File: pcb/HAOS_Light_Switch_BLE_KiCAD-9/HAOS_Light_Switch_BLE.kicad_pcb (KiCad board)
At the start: 2 copper layers, 30.1 x 29.9 mm, 34 parts, among them J1 GPIO, J2 GPIO, J3 GPIO, J4 Battery_CR2032, J7 SWD, SW1 SW_Push, SW2 SW_Push, SW3 SW_Push, U1 nrf52832, U3 RF_Antenna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

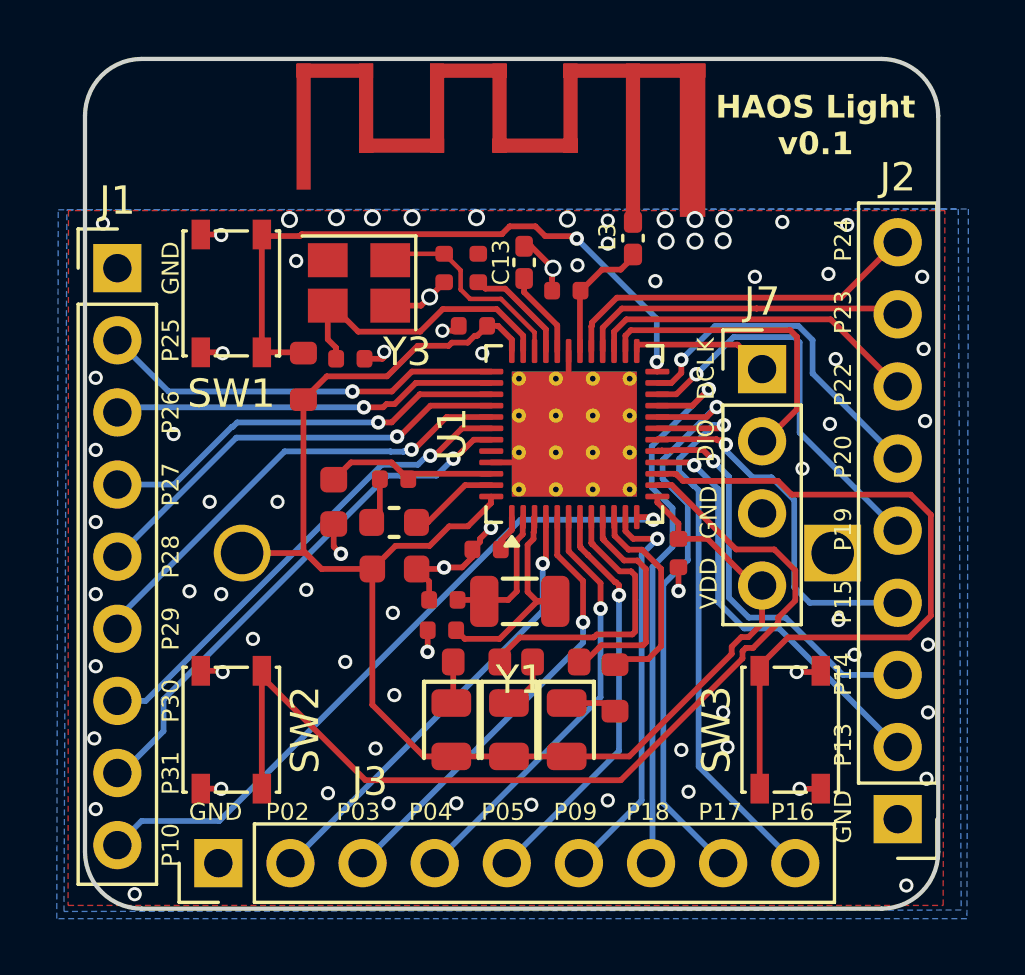
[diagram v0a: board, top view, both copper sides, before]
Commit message: Updated antenna
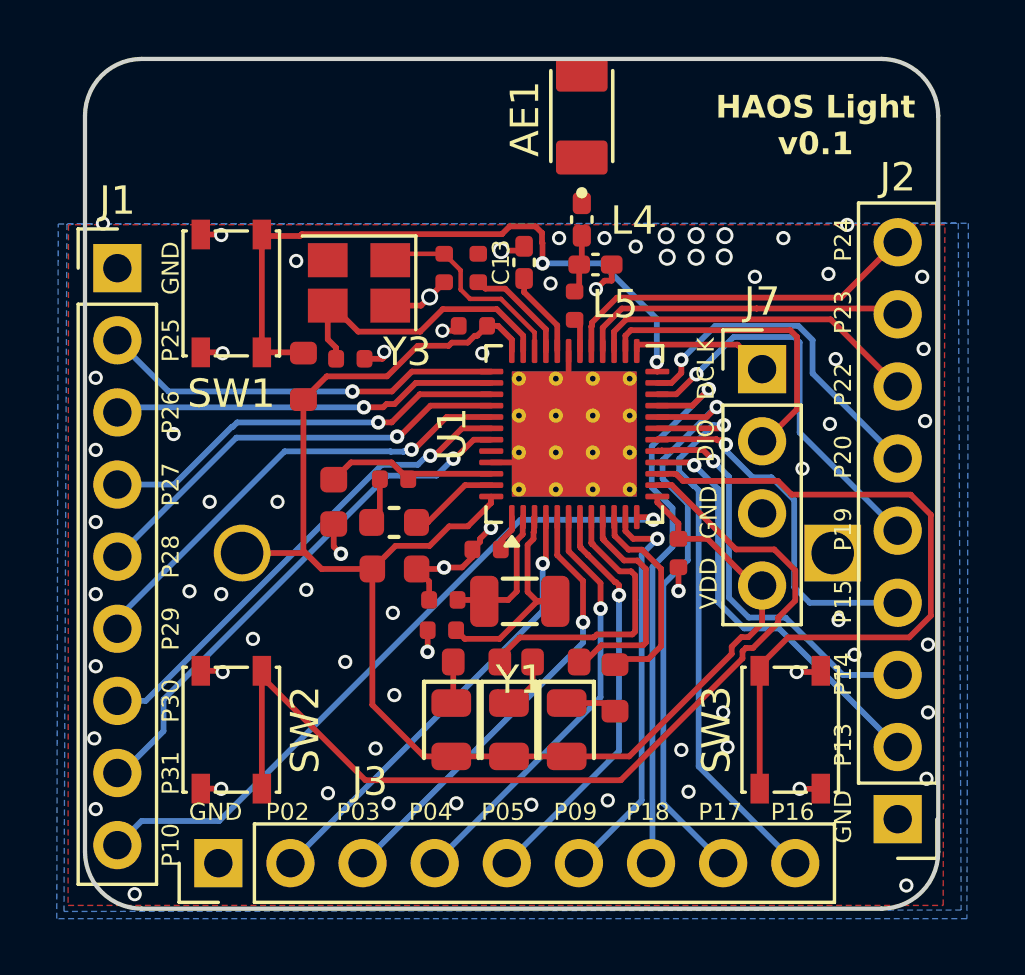
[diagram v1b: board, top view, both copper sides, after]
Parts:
- removed C14: 0.8pF, PCM_JLCPCB:C_0402
- removed L3: 3.9uH, Inductor_SMD:L_0402_1005Metric_Pad0.77x0.64mm_HandSolder
- removed U3: RF_Antenna, Footprints:Antenna-2.45GHZ_mirror
- added AE1: 2450AT18A100E, Footprints:ANTC3216X140N, F.Cu at (181.0, 106.4)
- added C3: 1pF, PCM_JLCPCB:C_0402, F.Cu at (180.7, 113.1)
- added L4: 3.9uH, Inductor_SMD:L_0402_1005Metric_Pad0.77x0.64mm_HandSolder, F.Cu at (181.0, 110.0)
- added L5: 2.7uH, Inductor_SMD:L_0402_1005Metric_Pad0.77x0.64mm_HandSolder, F.Cu at (181.5, 111.6)
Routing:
- net Net-(U1-ANT): track 4.57 -> 1.17 mm
- net Net-(C3-Pad2): track 0.00 -> 2.07 mm
- net /RESET: track 22.9 -> 23.6 mm
- net GND: vias 78 -> 73

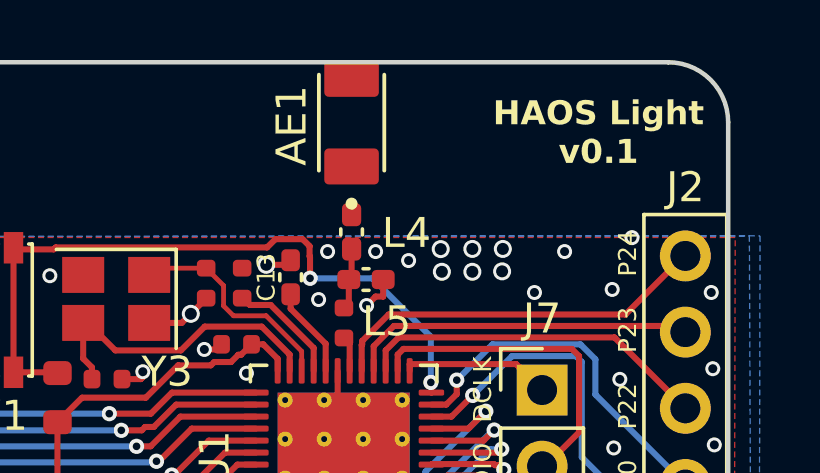
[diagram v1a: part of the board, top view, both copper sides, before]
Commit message: updated per DRC
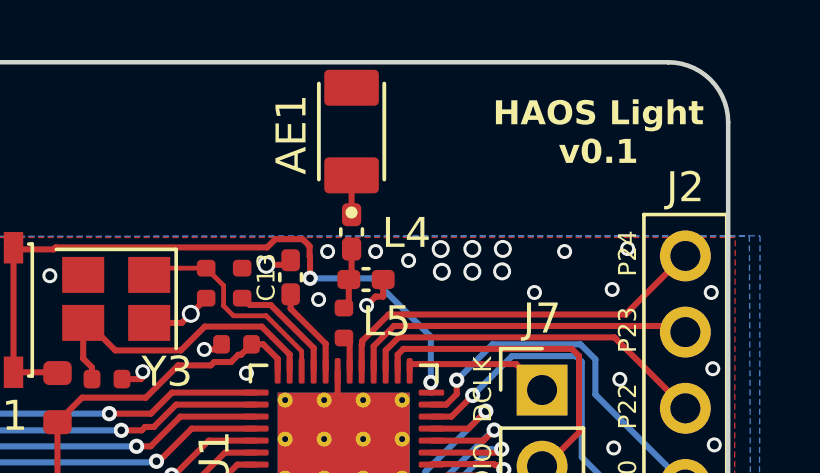
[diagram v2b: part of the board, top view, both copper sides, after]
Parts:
- moved AE1 0.30 mm to (181.0, 106.7)
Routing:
- net Net-(AE1-Pad1): track 0.00 -> 1.31 mm
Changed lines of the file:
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@@
 	(footprint "Footprints:ANTC3216X140N"
 		(layer "F.Cu")
-		(at 181 106.4032 90)
+		(at 181 106.7 90)
 		(property "Reference" "AE1"
 			(at -0.0968 -2 90)
@@
 	)
 	(via
-		(at 190.3476 110.236)
+		(at 190.2 110.6)
 		(size 0.5)
 		(drill 0.3)
@@
 	)
 	(segment
+		(start 181.0004 108.1604)
+		(end 181 108.16)
+		(width 0.2032)
+		(layer "F.Cu")
+		(net 44)
+	)
+	(segment
+		(start 181.0004 109.474)
+		(end 181.0004 108.1604)
+		(width 0.2032)
+		(layer "F.Cu")
+		(net 44)
+	)
+	(segment
 		(start 181.68927 125.0424)
 		(end 181.61127 125.1204)
@@
 		(min_thickness 0.254)
 		(filled_areas_thickness no)
-		(fill
+		(fill yes
 			(thermal_gap 0.508)
 			(thermal_bridge_width 0.508)
@@
 		(min_thickness 0.254)
 		(filled_areas_thickness no)
-		(fill
+		(fill yes
 			(thermal_gap 0.508)
 			(thermal_bridge_width 0.508)
@@
 		(min_thickness 0.254)
 		(filled_areas_thickness no)
-		(fill
+		(fill yes
 			(thermal_gap 0.508)
 			(thermal_bridge_width 0.508)

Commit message: Potential 1st spin.
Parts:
- added J5: PWR, Connector_PinHeader_1.00mm:PinHeader_1x02_P1.00mm_Vertical, F.Cu at (167.6, 117.1)
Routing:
- net VDD: track 54.2 -> 61.5 mm
- net /P0.27: track 14.5 -> 15.6 mm
- net /P0.26: track 13.6 -> 14.4 mm
- net GND: vias 73 -> 71
